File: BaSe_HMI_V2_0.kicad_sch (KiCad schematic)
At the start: 28 parts

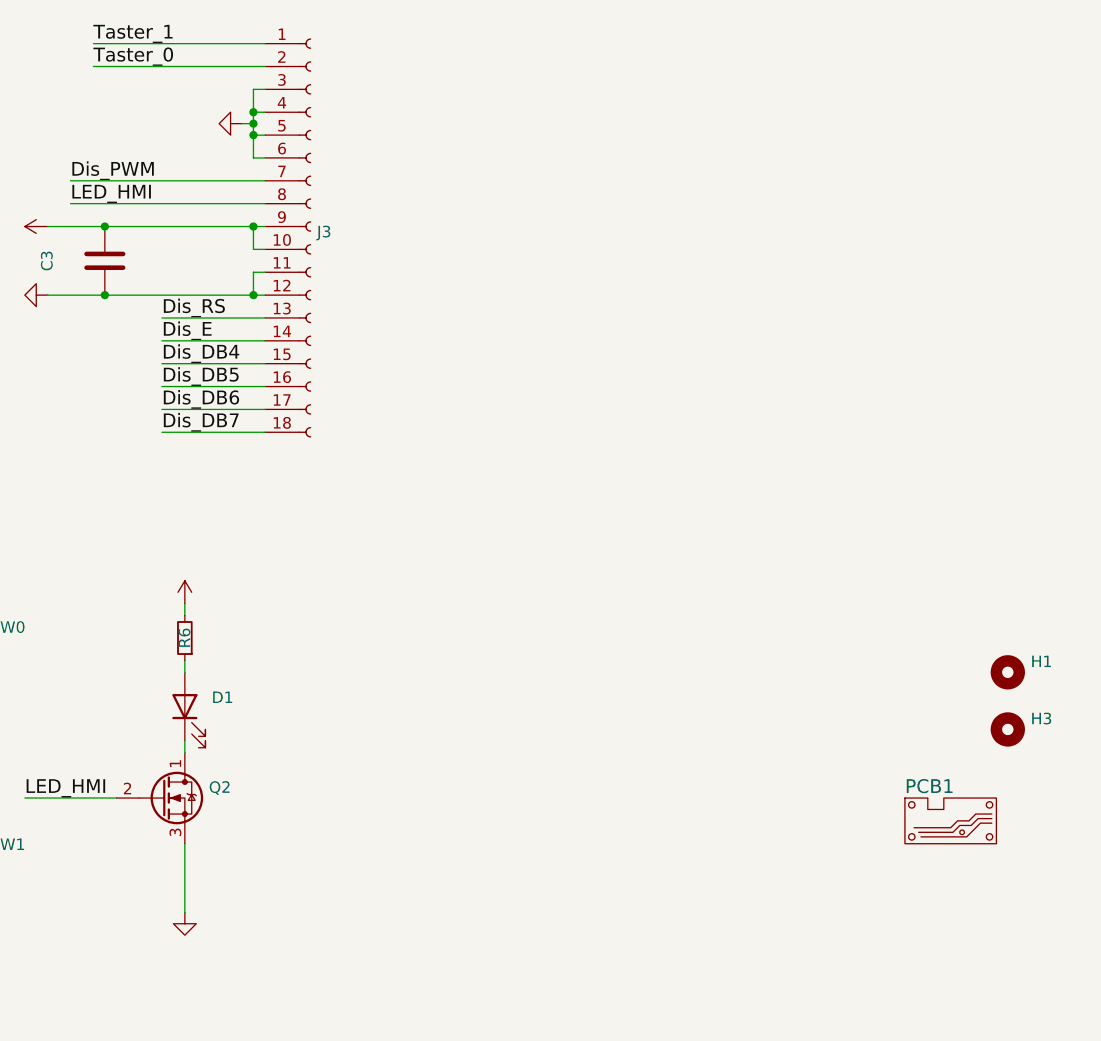
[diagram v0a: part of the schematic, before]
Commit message: beginning of v2.0. add PE and encoder
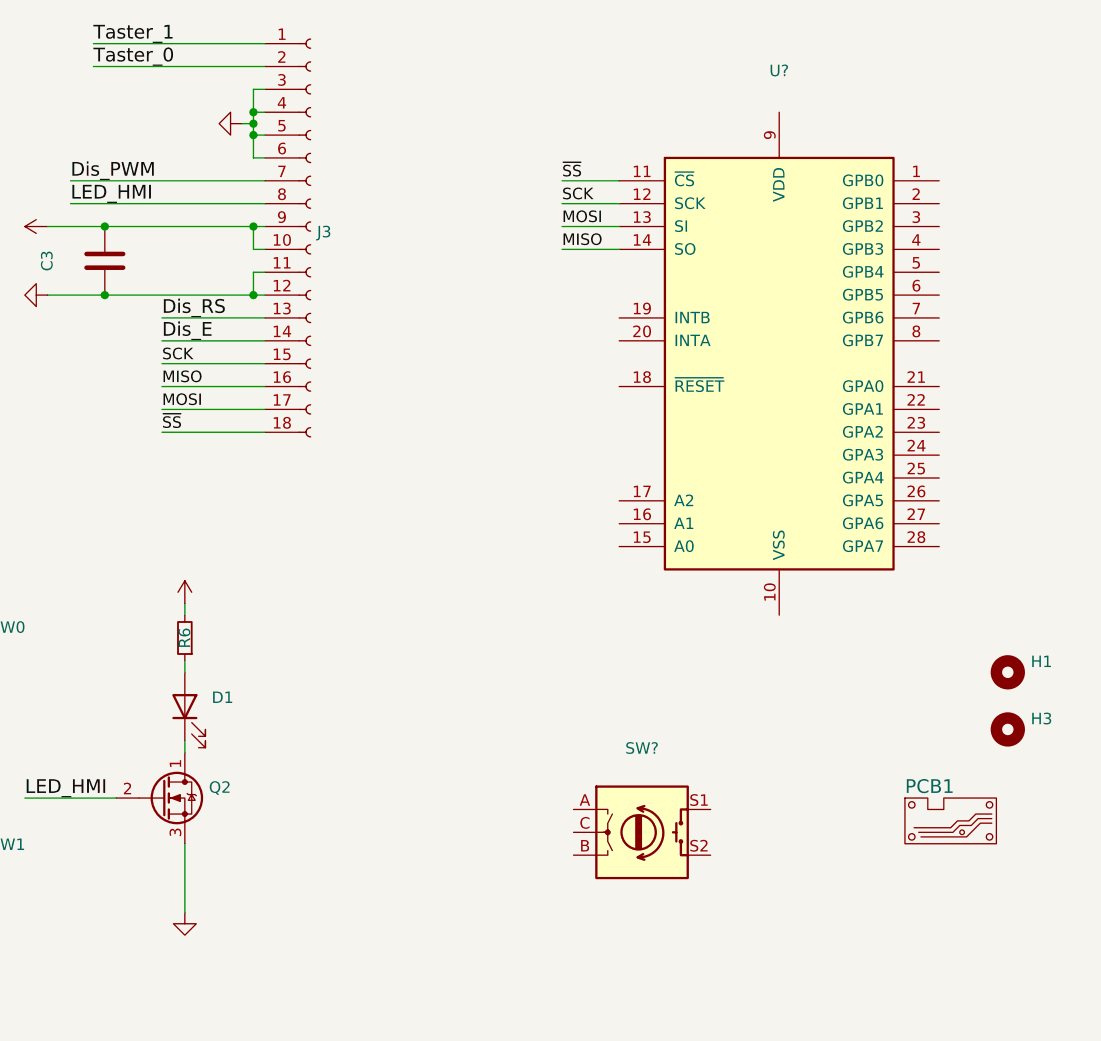
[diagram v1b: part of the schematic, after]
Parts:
- added SW?: (no value), symbol Device:Rotary_Encoder_Switch
- added U?: (no value), symbol Interface_Expansion:MCP23S17_SO
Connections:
- net Dis_DB4: no longer J3.15 (Pin_15)
- net Dis_DB5: no longer J3.16 (Pin_16)
- net Dis_DB6: no longer J3.17 (Pin_17)
- net Dis_DB7: no longer J3.18 (Pin_18)
- new net MISO: J3.16 (Pin_16), U?.14 (SO)
- new net MOSI: J3.17 (Pin_17), U?.13 (SI)
- new net SCK: J3.15 (Pin_15), U?.12 (SCK)
- new net ~{SS}: J3.18 (Pin_18), U?.11 (~{CS})
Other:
- title: BaSe_HMI_V1_1 -> BaSe_HMI_V2_0
